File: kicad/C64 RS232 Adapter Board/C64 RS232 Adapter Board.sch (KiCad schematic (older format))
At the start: 13 parts

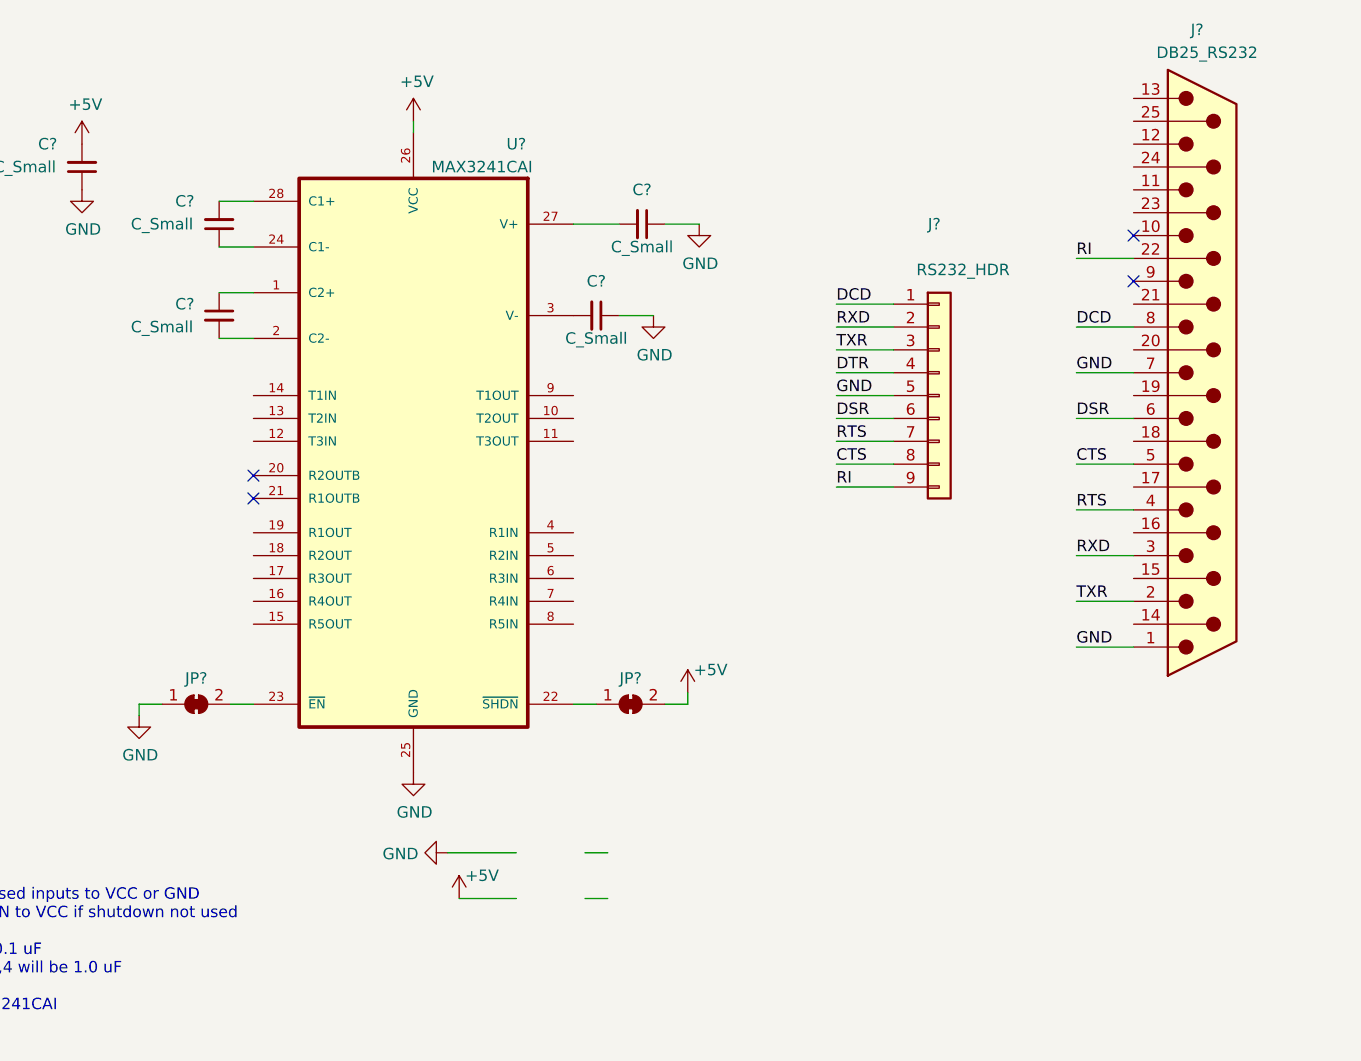
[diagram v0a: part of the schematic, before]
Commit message: Replaced with ESD version of 3241
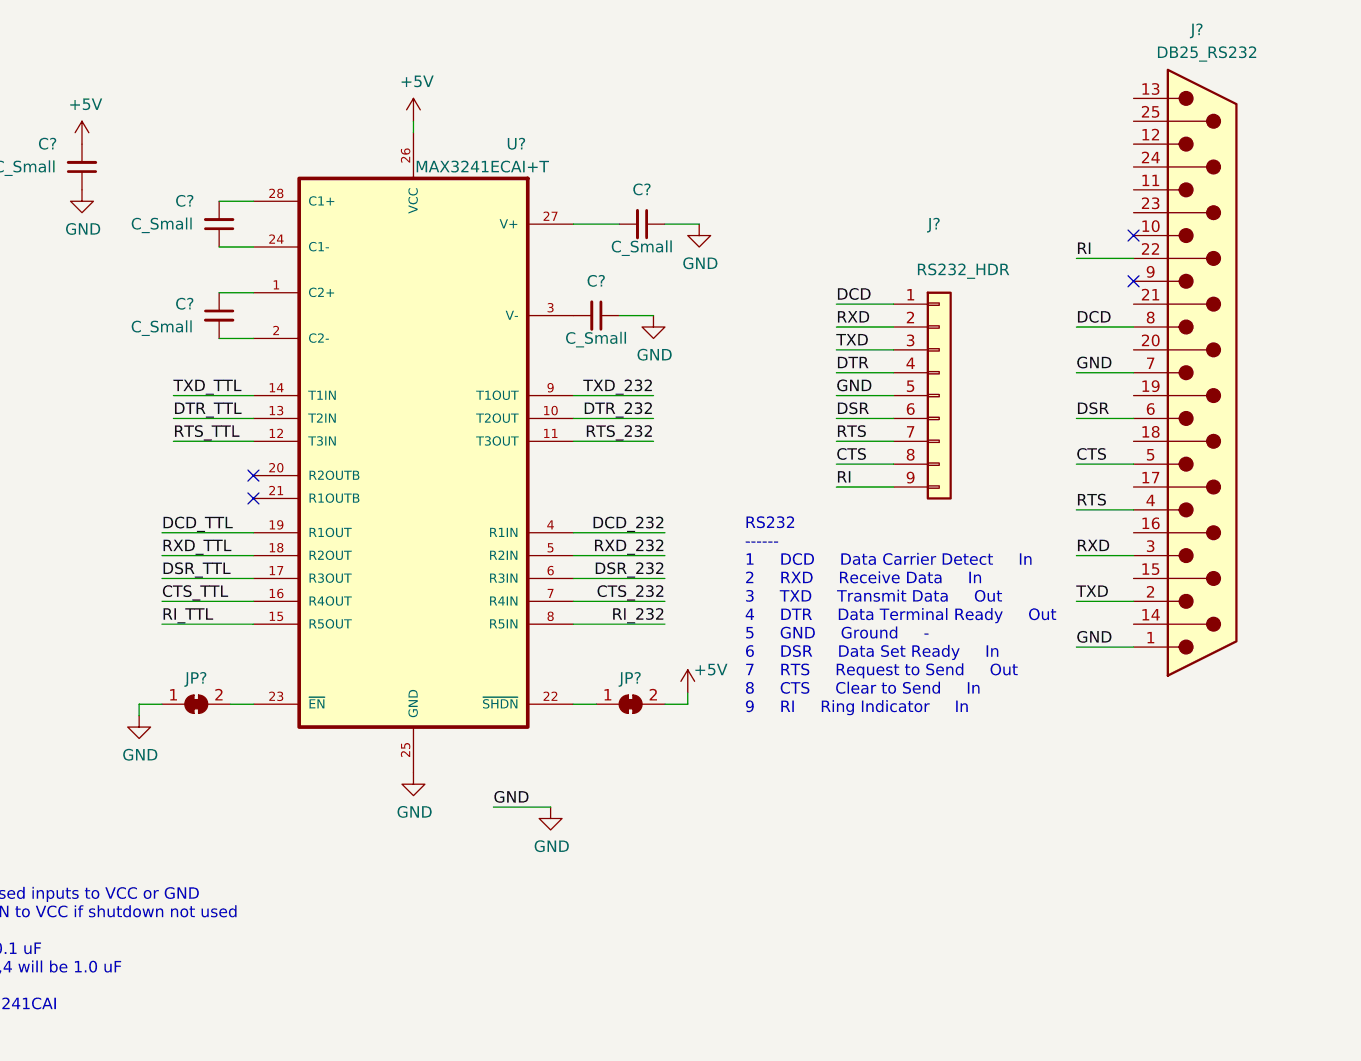
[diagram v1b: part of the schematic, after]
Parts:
- U?: value MAX3241CAI -> MAX3241ECAI+T; footprint SOP65P777X199-28N -> Package_SO:SSOP-28_5.3x10.2mm_P0.65mm; SPN (none) -> 73Y3495; Supplier (none) -> Newark
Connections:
- net labels added: CTS_232, CTS_TTL, DCD_232, DCD_TTL, DSR_232, DSR_TTL, DTR_232, DTR_TTL, RI_232, RI_TTL, RTS_232, RTS_TTL, RXD_232, RXD_TTL, TXD, TXD_232, TXD_TTL
- net labels removed: TXR
- wire segments 38 -> 51
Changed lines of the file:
@@
 RXD
 Text Label 7200 2250 0    50   ~ 0
-TXR
+TXD
 Text Label 7200 2350 0    50   ~ 0
 DTR
@@
 	8500 3150 8250 3150
 Text Label 8250 3350 0    50   ~ 0
-TXR
+TXD
 Wire Wire Line
 	8500 3350 8250 3350
@@
 P 5350 2800
 F 0 "U?" H 5800 4250 50  0000 C CNN
-F 1 "MAX3241CAI" H 5650 4150 50  0000 C CNN
-F 2 "SOP65P777X199-28N" H 4850 1500 50  0001 L BNN
-F 3 "" H 5350 2800 50  0001 C CNN
+F 1 "MAX3241ECAI+T" H 5650 4150 50  0000 C CNN
+F 2 "Package_SO:SSOP-28_5.3x10.2mm_P0.65mm" H 4850 1500 50  0001 L BNN
+F 3 "https://datasheet.octopart.com/MAX3241ECAI%2BT-Maxim-Integrated-datasheet-41193774.pdf" H 5350 2800 50  0001 C CNN
+F 4 "Newark" H 5350 2800 50  0001 C CNN "Supplier"
+F 5 "73Y3495" H 5350 2800 50  0001 C CNN "SPN"
 	1    5350 2800
 	1    0    0    -1
@@
 	1    0    0    -1
 $EndComp
-Wire Wire Line
-	6100 4450 6200 4450
-Wire Wire Line
-	6100 4650 6200 4650
 $Comp
 L power:GND #PWR?
 U 1 1 5F1D184C
-P 5500 4450
-F 0 "#PWR?" H 5500 4200 50  0001 C CNN
-F 1 "GND" V 5505 4322 50  0000 R CNN
-F 2 "" H 5500 4450 50  0001 C CNN
-F 3 "" H 5500 4450 50  0001 C CNN
-	1    5500 4450
-	0    1    1    0
-$EndComp
-Wire Wire Line
-	5800 4650 5550 4650
-$Comp
-L power:+5V #PWR?
-U 1 1 5F1D304D
-P 5550 4650
-F 0 "#PWR?" H 5550 4500 50  0001 C CNN
-F 1 "+5V" H 5650 4750 50  0000 C CNN
-F 2 "" H 5550 4650 50  0001 C CNN
-F 3 "" H 5550 4650 50  0001 C CNN
-	1    5550 4650
-	1    0    0    -1
-$EndComp
-Wire Wire Line
-	5500 4450 5800 4450
+P 5950 4250
+F 0 "#PWR?" H 5950 4000 50  0001 C CNN
+F 1 "GND" H 5955 4077 50  0000 C CNN
+F 2 "" H 5950 4250 50  0001 C CNN
+F 3 "" H 5950 4250 50  0001 C CNN
+	1    5950 4250
+	1    0    0    -1
+$EndComp
 Wire Wire Line
 	4650 1600 4500 1600
@@
 Wire Wire Line
 	6550 3800 6550 3750
+Text Notes 6800 3850 0    50   ~ 0
+RS232\n------\n1 	DCD 	Data Carrier Detect 	In\n2 	RXD 	Receive Data 	In\n3 	TXD 	Transmit Data 	Out\n4 	DTR 	Data Terminal Ready 	Out\n5 	GND 	Ground 	-\n6 	DSR 	Data Set Ready 	In\n7 	RTS 	Request to Send 	Out\n8 	CTS 	Clear to Send 	In\n9 	RI 	Ring Indicator 	In
+Text Label 6450 3050 2    50   ~ 0
+DCD_232
+Text Label 6450 3150 2    50   ~ 0
+RXD_232
+Text Label 6450 3250 2    50   ~ 0
+DSR_232
+Text Label 4300 2450 0    50   ~ 0
+TXD_TTL
+Text Label 4300 2550 0    50   ~ 0
+DTR_TTL
+Text Label 5700 4250 0    50   ~ 0
+GND
+Wire Wire Line
+	5950 4250 5700 4250
+Text Label 4300 2650 0    50   ~ 0
+RTS_TTL
+Text Label 6450 3350 2    50   ~ 0
+CTS_232
+Text Label 6450 3450 2    50   ~ 0
+RI_232
+Wire Wire Line
+	4300 2450 4650 2450
+Wire Wire Line
+	4300 2550 4650 2550
+Wire Wire Line
+	4300 2650 4650 2650
+Text Label 6400 2450 2    50   ~ 0
+TXD_232
+Text Label 6400 2550 2    50   ~ 0
+DTR_232
+Text Label 6400 2650 2    50   ~ 0
+RTS_232
+Wire Wire Line
+	6400 2450 6050 2450
+Wire Wire Line
+	6400 2550 6050 2550
+Wire Wire Line
+	6400 2650 6050 2650
+Wire Wire Line
+	6050 3050 6450 3050
+Wire Wire Line
+	6450 3150 6050 3150
+Wire Wire Line
+	6050 3250 6450 3250
+Wire Wire Line
+	6450 3350 6050 3350
+Wire Wire Line
+	6050 3450 6450 3450
+Text Label 4250 3050 0    50   ~ 0
+DCD_TTL
+Text Label 4250 3150 0    50   ~ 0
+RXD_TTL
+Text Label 4250 3250 0    50   ~ 0
+DSR_TTL
+Text Label 4250 3350 0    50   ~ 0
+CTS_TTL
+Text Label 4250 3450 0    50   ~ 0
+RI_TTL
+Wire Wire Line
+	4650 3050 4250 3050
+Wire Wire Line
+	4250 3150 4650 3150
+Wire Wire Line
+	4650 3250 4250 3250
+Wire Wire Line
+	4250 3350 4650 3350
+Wire Wire Line
+	4650 3450 4250 3450
 $EndSCHEMATC

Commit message: Finished schematic
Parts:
- removed J?: Blue Connect to C64, symbol Connector_Generic:Conn_02x12_Top_Bottom
- removed J?: Break-outfor User Port, symbol Connector_Generic:Conn_02x12_Top_Bottom
- removed JP?: SolderJumper_2_Bridged, symbol Jumper:SolderJumper_2_Bridged
- added D?: PWR, LED_SMD:LED_1206_3216Metric, symbol Device:LED_Small
- added H? (x4): MountingHole, MountingHole:MountingHole_2.5mm, symbol Mechanical:MountingHole
- added J?: C64_USER_PORT, symbol C64_RS232_Adapter_Library:C64_USER_PORT
- added J?: User Port Breakout, symbol C64_RS232_Adapter_Library:C64_USER_PORT
- added JP? (x11): SolderJumper_2_Bridged, symbol Jumper:SolderJumper_2_Bridged
- added R?: 10K, Resistor_SMD:R_0805_2012Metric, symbol Device:R_Small
- added R?: 1K, Resistor_SMD:R_0805_2012Metric, symbol Device:R_Small
- added SW?: RESET, symbol Switch:SW_SPST
- C1: renamed from C?; value C_Small -> 0.1u
- C2, C3, C4: renamed from C?; value C_Small -> 1u
- C?: value C_Small -> 1u
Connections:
- net labels added: +9VAC, -9VAC, ATN, CNT1, CNT2, FLAG2, PA2, PB0, PB1, PB2, PB3, PB4, PB5, PB6, PB7, PC2, RESET, SP1, SP2
- net labels removed: C64_B, CD, CTS, DCD, DSR, DTR, RI, RTS, RXD, TXD
- wire segments 51 -> 116
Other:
- note added: "Esp8266 GND -> C64 User Port Pin N (Gnd)\nEsp8266 TxD (GPIO1/TXD0) -> C64 User Port B and C (RxD. Yes, Short B and C together)\nEsp8266 RxD (GPIO3/RXD0) -> C64 User Port M (TxD)\nEsp8266 GPIO4 -> C64 User Port K (CTS)\nEsp8266 GPIO5 -> C64 User Port D (RTS)\nEsp8266 GPIO2 (d4) -> User Port H (DCD)\n\nThen:\n\nAdd a wire from M to 5 on user port plug\nAdd a wire from B,C to 7 on user port plug\nAd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"
- note removed: "- Unused inputs to VCC or GND\n- SHTN to VCC if shutdown not used\n\n-C1: 0.1 uF\n-C2,3,4 will be 1.0 uF\n\nMAX3241CAI"
- moved on the sheet: C1, C2, C3, C4, C?, J?, JP?, U?

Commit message: Finalized footprints, annotated, ready for PCB
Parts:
- J1: renamed from J?; footprint (none) -> Connector_PinHeader_2.54mm:PinHeader_1x10_P2.54mm_Vertical
- J2: renamed from J?; footprint (none) -> Connector_Dsub:DSUB-25_Male_EdgeMount_P2.77mm
- J3: renamed from J?; footprint (none) -> My Libraries:0.156-2x12
- J4: renamed from J?; footprint (none) -> My Libraries:TSM-112-01-L-DV; MFN (none) -> 15-91-0240; Manu (none) -> Molex; SPN (none) -> 25M0665
- JP1, JP10, JP11, JP12, JP13, JP2, JP3, JP4, JP5, JP6, JP7, JP8, JP9: renamed from JP?; footprint (none) -> Jumper:SolderJumper-2_P1.3mm_Bridged_RoundedPad1.0x1.5mm
- SW1: renamed from SW?; footprint (none) -> My Libraries:Pushbutton-SMD-TL3305-2-Pad
- U1: renamed from U?; symbol My_Library:MAX3241CAI -> C64-RS232-Adapter-Board-rescue:MAX3241CAI-My_Library
- gave numbers to parts that had none: 8

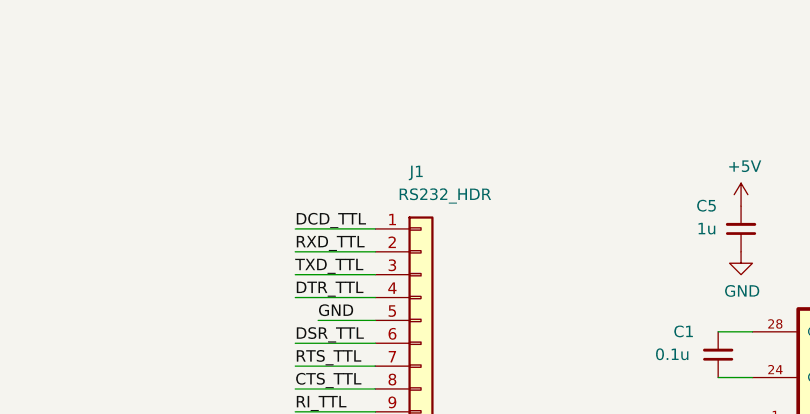
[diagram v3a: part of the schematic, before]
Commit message: First pass of part layout
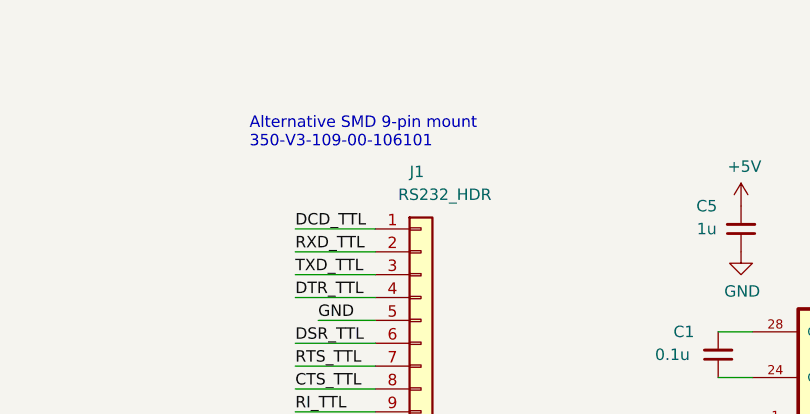
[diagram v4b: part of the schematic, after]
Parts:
- J4: footprint My Libraries:TSM-112-01-L-DV -> My Libraries:TSM-for-C64-User-Port
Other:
- note added: "Alternative SMD 9-pin mount\n350-V3-109-00-106101"
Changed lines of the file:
@@
 F 0 "J4" H 3975 4120 50  0000 C CNN
 F 1 "User Port Breakout" H 3975 4029 50  0000 C CNN
-F 2 "My Libraries:TSM-112-01-L-DV" H 3950 3350 50  0001 C CNN
+F 2 "My Libraries:TSM-for-C64-User-Port" H 3950 3350 50  0001 C CNN
 F 3 "https://sigma.octopart.com/11591496/technical_drawing/Molex-15-91-0240.pdf" H 3950 3350 50  0001 C CNN
 F 4 "Molex" H 3950 3350 50  0001 C CNN "Manu"
@@
 	1    0    0    -1
 $EndComp
+Text Notes 5150 1400 0    50   ~ 0
+Alternative SMD 9-pin mount\n350-V3-109-00-106101
 $EndSCHEMATC

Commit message: Tried this layout but don't like it
Instead of going a 2nd time, going to try creating two boards instead
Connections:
- net RESET: now also R2.2, SW1.1 (A)
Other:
- note added: "Alternative SMD 9-pin mount\n350-V3-109-00-106101\noR A 10 PIN: \n10129380-910001ALF"
- note removed: "Alternative SMD 9-pin mount\n350-V3-109-00-106101"
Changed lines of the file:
@@
 $EndComp
 Text Notes 5150 1400 0    50   ~ 0
-Alternative SMD 9-pin mount\n350-V3-109-00-106101
+Alternative SMD 9-pin mount\n350-V3-109-00-106101\noR A 10 PIN: \n10129380-910001ALF
+Text Label 1400 1750 1    50   ~ 0
+RESET
 $EndSCHEMATC
